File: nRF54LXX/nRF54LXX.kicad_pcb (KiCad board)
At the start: 4 copper layers, 49.2 x 40 mm, 24 parts, among them IC1 NRF54L15-QFAA-R7, J1 MM8130-2600RA2, J2 Programmer, Y1 32.768kHz, Y2 32MHz

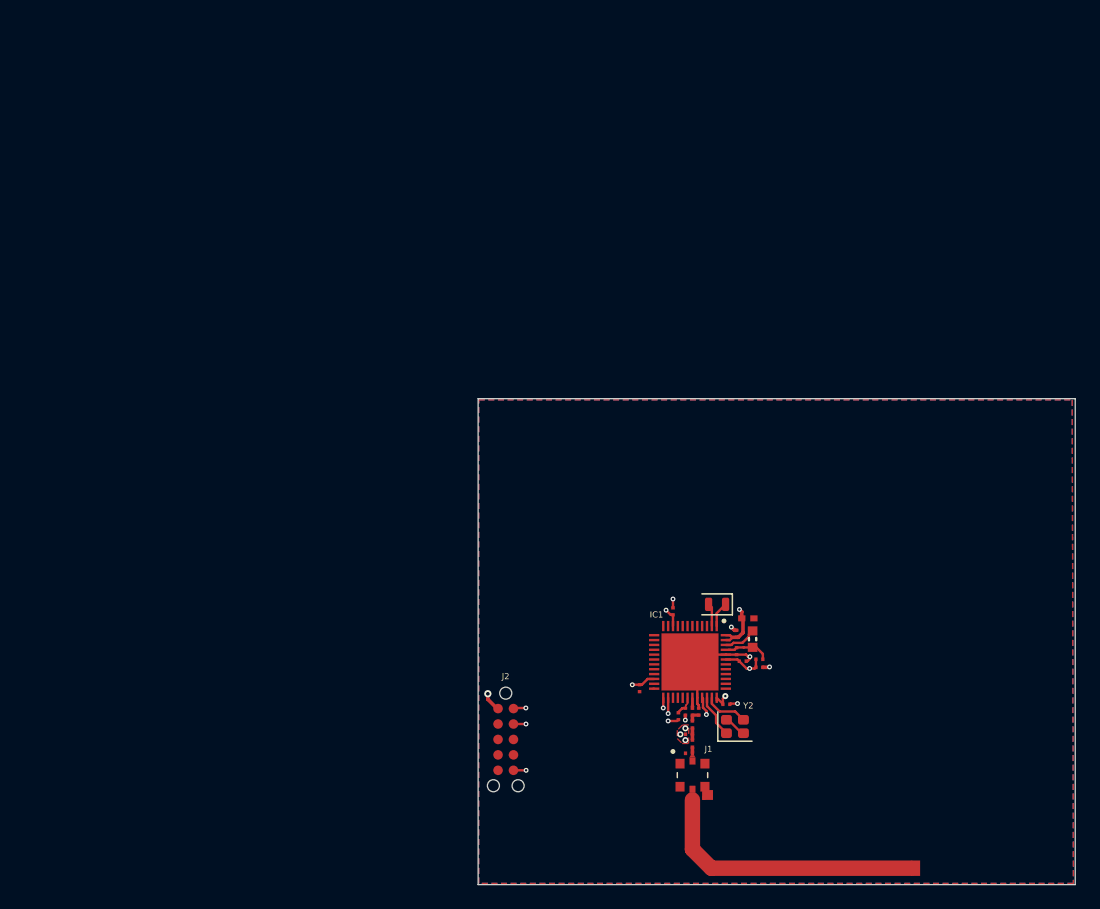
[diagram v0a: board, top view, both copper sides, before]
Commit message: Updated Schematic to increase readability
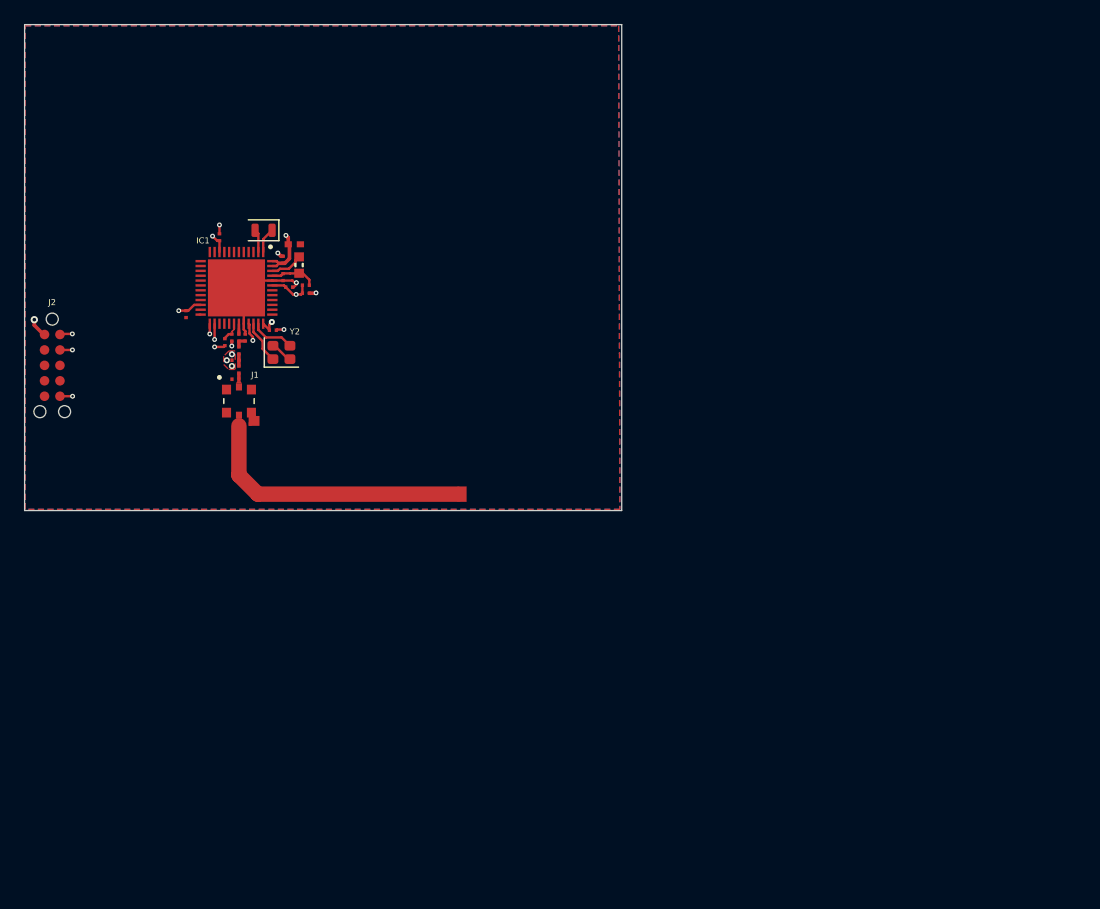
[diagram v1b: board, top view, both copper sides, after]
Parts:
- moved C7 48.4 mm to (100.3, 64.0)
- moved C9 48.4 mm to (94.2, 67.7)
- moved J1 48.4 mm to (94.8, 72.9)
- moved R1 48.4 mm to (93.7, 68.1)
- moved C1 48.4 mm to (99.4, 60.0)
- moved C3 48.4 mm to (90.5, 65.8)
- moved C5 48.4 mm to (98.4, 61.3)
- moved FB1 48.4 mm to (100.3, 63.4)
- moved C10 48.4 mm to (95.3, 67.7)
- moved C12 48.4 mm to (94.5, 71.1)
- moved C13 48.4 mm to (95.5, 74.8)
- moved C4 48.4 mm to (97.6, 67.1)
- moved J2 48.4 mm to (78.8, 67.4)
- moved L4 48.4 mm to (94.8, 70.3)
- moved C11 48.4 mm to (94.5, 69.6)
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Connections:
- C8 pad 1: Net-(IC1-DECD) -> Net-(IC1A-DECD)
- FB1 pad 2: Net-(IC1-DECD) -> Net-(IC1A-DECD)
- IC1 pad 45: Net-(IC1-DECD) -> Net-(IC1A-DECD)
- IC1 pad 46: Net-(IC1-DCC) -> Net-(IC1A-DCC)
- L1 pad 1: Net-(IC1-DECD) -> Net-(IC1A-DCC)
- L1 pad 2: Net-(IC1-DCC) -> Net-(IC1A-DECD)
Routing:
- net Net-(IC1A-DECD): track 0.00 -> 3.83 mm
- net Net-(IC1-DECD): track 3.61 -> 0.00 mm
- net Net-(IC1A-DCC): track 0.00 -> 2.75 mm
- net Net-(IC1-DCC): track 2.75 -> 0.00 mm
- net GND: track 15.1 -> 14.3 mm
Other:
- board size 49.2 x 40 mm -> 49.1 x 40 mm

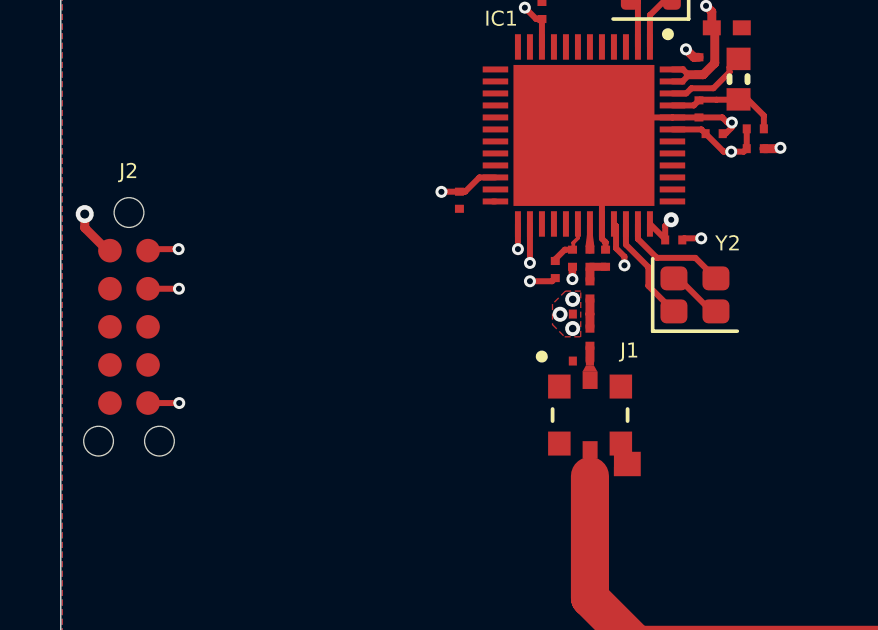
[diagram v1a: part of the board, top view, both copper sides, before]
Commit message: TC2050 programmer routed
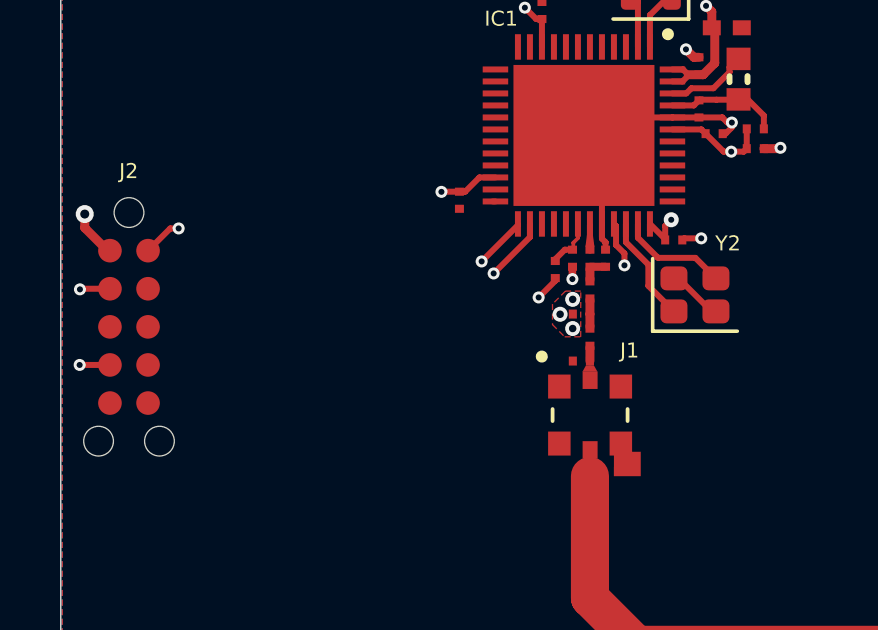
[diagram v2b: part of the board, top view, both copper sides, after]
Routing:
- net /SWDCLK: track 14.4 -> 18.2 mm
- net /SWDIO: track 13.2 -> 16.5 mm
- net /MCU_RST: track 16.9 -> 15.2 mm
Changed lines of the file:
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@@
 		(capping no)
 		(filling no)
-		(zone_defaults)
 		(pcbplotparams
 			(layerselection 0x00000000_00000000_55555555_5755f5ff)
@@
 		(sheetname "/")
 		(sheetfile "nRF54LXX.kicad_sch")
-		(units
-			(unit
-				(name "A")
-				(pins "1" "3" "5" "7" "9" "2" "4" "6" "8" "10")
-			)
-		)
 		(attr smd exclude_from_bom)
 		(duplicate_pad_numbers_are_jumpers no)
@@
 		)
 		(pad "2" smd circle
-			(at 1.27 0)
+			(at 0 1.27)
 			(size 0.787 0.787)
 			(layers "F.Cu" "F.Mask")
@@
 		)
 		(pad "3" smd circle
-			(at 0 1.27)
+			(at 0 2.54)
 			(size 0.787 0.787)
 			(layers "F.Cu" "F.Mask")
@@
 		)
 		(pad "4" smd circle
-			(at 1.27 1.27)
+			(at 0 3.81)
 			(size 0.787 0.787)
 			(layers "F.Cu" "F.Mask")
@@
 		)
 		(pad "5" smd circle
-			(at 0 2.54)
+			(at 0 5.08)
 			(size 0.787 0.787)
 			(layers "F.Cu" "F.Mask")
@@
 		)
 		(pad "6" smd circle
-			(at 1.27 2.54)
+			(at 1.27 5.08)
 			(size 0.787 0.787)
 			(layers "F.Cu" "F.Mask")
@@
 		)
 		(pad "7" smd circle
-			(at 0 3.81)
+			(at 1.27 3.81)
 			(size 0.787 0.787)
 			(layers "F.Cu" "F.Mask")
@@
 		)
 		(pad "8" smd circle
-			(at 1.27 3.81)
+			(at 1.27 2.54)
 			(size 0.787 0.787)
 			(layers "F.Cu" "F.Mask")
@@
 		)
 		(pad "9" smd circle
-			(at 0 5.08)
+			(at 1.27 1.27)
 			(size 0.787 0.787)
 			(layers "F.Cu" "F.Mask")
@@
 		)
 		(pad "10" smd circle
-			(at 1.27 5.08)
+			(at 1.27 0)
 			(size 0.787 0.787)
 			(layers "F.Cu" "F.Mask")
@@
 	)
 	(segment
-		(start 81.1 67.39)
-		(end 80.13 67.39)
+		(start 92.41 66.59)
+		(end 92.41 66.55)
 		(width 0.2)
 		(layer "F.Cu")
@@
 	)
 	(segment
-		(start 80.13 67.39)
-		(end 80.08 67.44)
+		(start 77.81 68.73)
+		(end 77.83 68.71)
 		(width 0.2)
 		(layer "F.Cu")
@@
 	)
 	(segment
-		(start 92.41 67.39)
-		(end 92.41 66.55)
+		(start 77.83 68.71)
+		(end 78.81 68.71)
+		(width 0.2)
+		(layer "F.Cu")
+		(net "/SWDIO")
+	)
+	(segment
+		(start 91.2 67.8)
+		(end 92.41 66.59)
 		(width 0.2)
 		(layer "F.Cu")
@@
 	)
 	(via
-		(at 81.1 67.39)
+		(at 77.81 68.73)
 		(size 0.4)
 		(drill 0.2)
@@
 	)
 	(via
-		(at 92.41 67.39)
+		(at 91.2 67.8)
 		(size 0.4)
 		(drill 0.2)
@@
 	)
 	(segment
-		(start 92.41 67.39)
-		(end 81.1 67.39)
+		(start 90.3 68.7)
+		(end 77.84 68.7)
+		(width 0.2)
+		(layer "In1.Cu")
+		(net "/SWDIO")
+	)
+	(segment
+		(start 91.2 67.8)
+		(end 90.3 68.7)
+		(width 0.2)
+		(layer "In1.Cu")
+		(net "/SWDIO")
+	)
+	(segment
+		(start 77.84 68.7)
+		(end 77.81 68.73)
 		(width 0.2)
 		(layer "In1.Cu")
@@
 	)
 	(segment
-		(start 92.81 67.85)
-		(end 92.81 66.55)
+		(start 91.6 68.2)
+		(end 92.81 66.99)
+		(width 0.2)
+		(layer "F.Cu")
+		(net "/SWDCLK")
+	)
+	(segment
+		(start 77.8 71.25)
+		(end 78.81 71.25)
 		(width 0.2)
 		(layer "F.Cu")
@@
 	)
 	(segment
-		(start 81.11 68.71)
-		(end 80.08 68.71)
+		(start 92.81 66.99)
+		(end 92.81 66.55)
 		(width 0.2)
 		(layer "F.Cu")
@@
 	)
 	(via
-		(at 92.81 67.85)
+		(at 91.6 68.2)
 		(size 0.4)
 		(drill 0.2)
@@
 	)
 	(via
-		(at 81.11 68.71)
+		(at 77.8 71.25)
 		(size 0.4)
 		(drill 0.2)
@@
 	)
 	(segment
-		(start 81.97 67.85)
-		(end 81.11 68.71)
+		(start 91.6 68.2)
+		(end 90.5 69.3)
 		(width 0.2)
 		(layer "In1.Cu")
@@
 	)
 	(segment
-		(start 92.81 67.85)
-		(end 81.97 67.85)
+		(start 90.5 69.3)
+		(end 79.75 69.3)
 		(width 0.2)
 		(layer "In1.Cu")
@@
 	)
 	(segment
-		(start 81.12 72.52)
-		(end 80.08 72.52)
+		(start 79.75 69.3)
+		(end 77.8 71.25)
+		(width 0.2)
+		(layer "In1.Cu")
+		(net "/SWDCLK")
+	)
+	(segment
+		(start 80.82 66.7)
+		(end 80.08 67.44)
 		(width 0.2)
 		(layer "F.Cu")
@@
 	)
 	(segment
-		(start 92.81 68.46)
-		(end 93.54965 68.46)
+		(start 93.65499 68.44501)
+		(end 93.1 69)
 		(width 0.2)
 		(layer "F.Cu")
@@
 	)
 	(segment
-		(start 93.54965 68.46)
-		(end 93.65499 68.35466)
+		(start 81.1 66.7)
+		(end 80.82 66.7)
+		(width 0.2)
+		(layer "F.Cu")
+		(net "/MCU_RST")
+	)
+	(segment
+		(start 93.65499 68.35466)
+		(end 93.65499 68.44501)
 		(width 0.2)
 		(layer "F.Cu")
@@
 	)
 	(via
-		(at 92.81 68.46)
+		(at 93.1 69)
 		(size 0.4)
 		(drill 0.2)
 		(layers "F.Cu" "B.Cu")
-		(free yes)
 		(net "/MCU_RST")
 	)
 	(via
-		(at 81.12 72.52)
+		(at 81.1 66.7)
 		(size 0.4)
 		(drill 0.2)
@@
 	)
 	(segment
-		(start 92.81 68.46)
-		(end 82.42 68.46)
+		(start 90.865686 66.7)
+		(end 81.1 66.7)
 		(width 0.2)
 		(layer "In1.Cu")
@@
 	)
 	(segment
-		(start 81.12 69.76)
-		(end 81.12 72.52)
+		(start 93.1 69)
+		(end 93.1 68.934314)
 		(width 0.2)
 		(layer "In1.Cu")
@@
 	)
 	(segment
-		(start 82.42 68.46)
-		(end 81.12 69.76)
+		(start 93.1 68.934314)
+		(end 90.865686 66.7)
 		(width 0.2)
 		(layer "In1.Cu")
@@
 	)
 	(segment
-		(start 97.61 69.465)
-		(end 96.7575 68.6125)
+		(start 96.01 67.16)
+		(end 96.01 66.55)
 		(width 0.2)
 		(layer "F.Cu")
@@
 	)
 	(segment
-		(start 96.01 67.24)
-		(end 96.01 66.55)
+		(start 97.61 69.465)
+		(end 96.7575 68.6125)
 		(width 0.2)
 		(layer "F.Cu")
@@
 	)
 	(segment
-		(start 96.7575 67.9875)
-		(end 96.01 67.24)
+		(start 96.7575 68.6125)
+		(end 96.7575 67.9075)
 		(width 0.2)
 		(layer "F.Cu")
@@
 	)
 	(segment
-		(start 96.7575 68.6125)
-		(end 96.7575 67.9875)
+		(start 96.7575 67.9075)
+		(end 96.01 67.16)
 		(width 0.2)
 		(layer "F.Cu")
@@
 	)
 	(segment
-		(start 97.04 67.68)
-		(end 96.41 67.05)
+		(start 98.325 67.68)
+		(end 97.08 67.68)
 		(width 0.2)
 		(layer "F.Cu")
@@
 	)
 	(segment
-		(start 99.01 68.365)
-		(end 98.325 67.68)
+		(start 96.41 67.01)
+		(end 96.41 66.55)
 		(width 0.2)
 		(layer "F.Cu")
@@
 	)
 	(segment
-		(start 96.41 67.05)
-		(end 96.41 66.55)
+		(start 97.08 67.68)
+		(end 96.41 67.01)
 		(width 0.2)
 		(layer "F.Cu")
@@
 	)
 	(segment
-		(start 98.325 67.68)
-		(end 97.04 67.68)
+		(start 99.01 68.365)
+		(end 98.325 67.68)
 		(width 0.2)
 		(layer "F.Cu")
@@
 	)
 	(segment
-		(start 95.67999 67.35999)
-		(end 95.67999 66.61999)
+		(start 95.96 67.534264)
+		(end 95.67999 67.254254)
 		(width 0.2)
 		(layer "F.Cu")
@@
 	)
 	(segment
-		(start 95.67999 66.61999)
-		(end 95.61 66.55)
+		(start 95.96 67.93)
+		(end 95.96 67.534264)
 		(width 0.2)
 		(layer "F.Cu")
@@
 	)
 	(segment
+		(start 95.67999 66.61999)
+		(end 95.61 66.55)
+		(width 0.2)
+		(layer "F.Cu")
+		(net "Net-(IC1A-DECA)")
+	)
+	(segment
 		(start 97.55999 63.4)
 		(end 98.525 63.4)
@@
 	)
 	(segment
-		(start 95.96 67.93)
-		(end 95.96 67.64)
+		(start 95.67999 67.254254)
+		(end 95.67999 66.61999)
 		(width 0.2)
 		(layer "F.Cu")
@@
 		(net "Net-(IC1A-DECA)")
 	)
-	(segment
-		(start 95.96 67.64)
-		(end 95.67999 67.35999)
-		(width 0.2)
-		(layer "F.Cu")
-		(net "Net-(IC1A-DECA)")
-	)
 	(via
 		(at 95.96 67.93)
@@
 	)
 	(zone
+		(layer "F.Cu")
+		(hatch edge 0.5)
+		(connect_pads
+			(clearance 0)
+		)
+		(min_thickness 0.25)
+		(keepout
+			(tracks allowed)
+			(vias allowed)
+			(pads allowed)
+			(copperpour not_allowed)
+			(footprints allowed)
+		)
+		(placement
+			(enabled no)
+			(sheetname "/")
+		)
+		(fill
+			(thermal_gap 0.5)
+			(thermal_bridge_width 0.5)
+			(island_removal_mode 0)
+		)
+		(polygon
+			(pts
+				(xy 80.1 67.44) (xy 78.81 67.44) (xy 78.81 72.6) (xy 80.1 72.6)
+			)
+		)
+	)
+	(zone
